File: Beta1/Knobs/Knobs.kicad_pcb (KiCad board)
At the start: 2 copper layers, 194 x 32.1 mm, 31 parts, among them U1000 MCP3008T-I/SL, U2 MCP3008T-I/SL

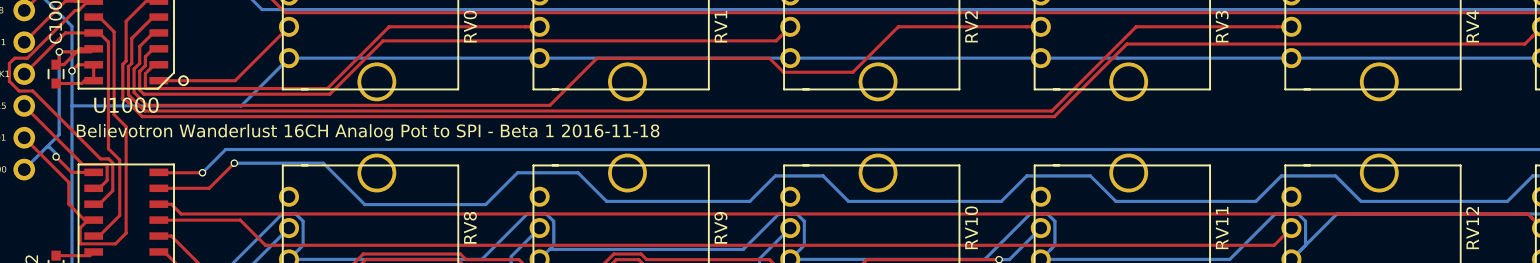
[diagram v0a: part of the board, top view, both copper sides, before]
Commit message: Housekeeping files. Renamed Knob with LED to Knobs. Board is ready for Gerbers.
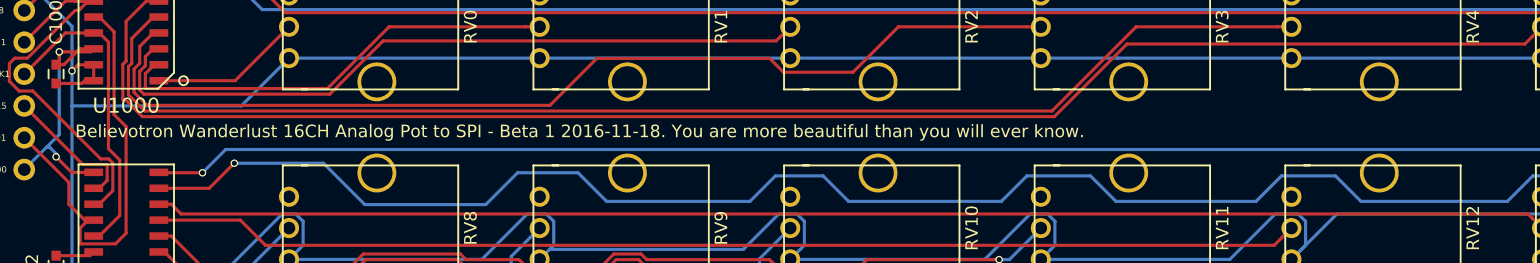
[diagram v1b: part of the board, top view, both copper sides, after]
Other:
- board text added: "Believotron Wanderlust 16CH Analog Pot to SPI - Beta 1 2016-11-18. You are more beautiful than you will ever know."
- board text removed: "Believotron Wanderlust 16CH Analog Pot to SPI - Beta 1 2016-11-18"
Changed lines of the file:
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@@
 (kicad_pcb (version 4) (host pcbnew 4.0.4-stable)
   (general
-    (links 0)
+    (links 68)
     (no_connects 0)
     (area -0.050001 -32.175001 194.010001 0.050001)
@@
     (pad "" np_thru_hole circle (at 0 0) (size 3.3 3.3) (drill 3.3) (layers *.Cu *.Mask))
   )
-  (gr_text "Believotron Wanderlust 16CH Analog Pot to SPI - Beta 1 2016-11-18" (at 11.684 -15.748) (layer F.SilkS)
+  (gr_text "Believotron Wanderlust 16CH Analog Pot to SPI - Beta 1 2016-11-18. You are more beautiful than you will ever know." (at 11.684 -15.748) (layer F.SilkS)
     (effects (font (size 1 1) (thickness 0.25)) (justify left))
   )

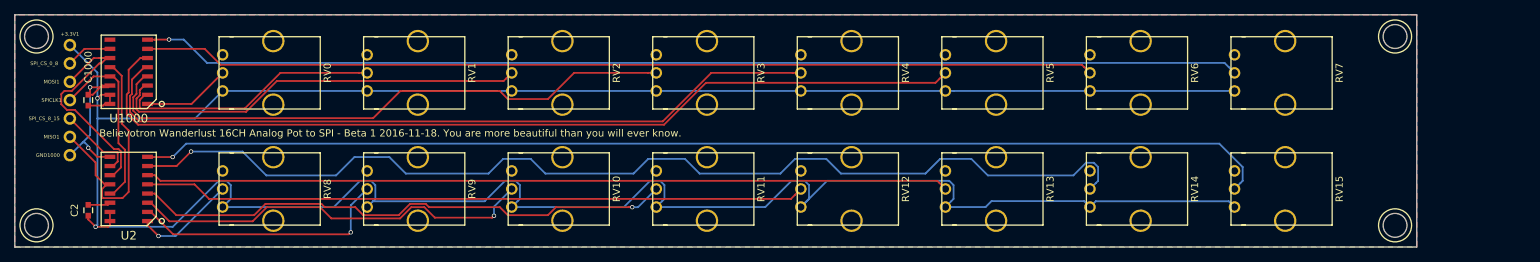
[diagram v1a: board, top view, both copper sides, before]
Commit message: Added second header row for easy daisychaining / interfacing
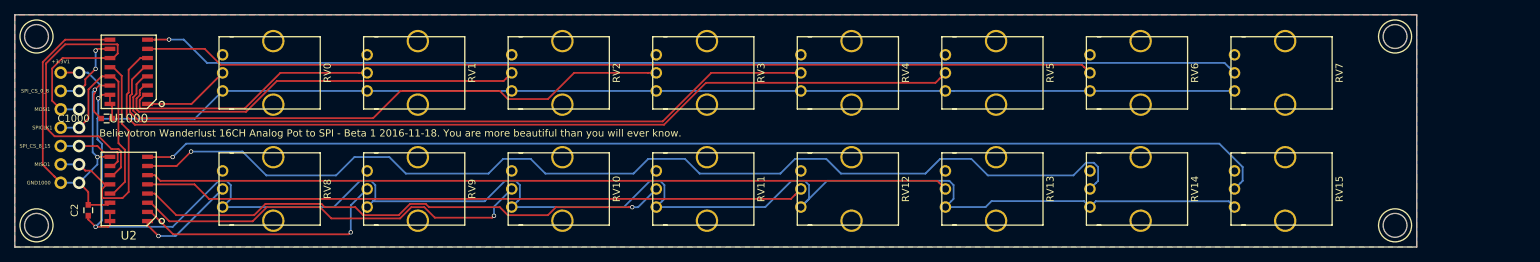
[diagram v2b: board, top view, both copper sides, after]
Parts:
- moved +3.3V1 4.02 mm to (6.35, -24.1)
- moved MISO1 4.02 mm to (6.35, -11.4)
- moved SPI_CS_8_15 4.02 mm to (6.35, -14.0)
- moved GND1000 4.02 mm to (6.35, -8.89)
- moved MOSI1 4.02 mm to (6.35, -19.1)
- moved SPICLK1 4.02 mm to (6.35, -16.5)
- moved SPI_CS_0_8 4.02 mm to (6.35, -21.6)
- moved C1000 3.59 mm to (12.7, -17.8), turned to 180 degrees
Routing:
- net GND: track 25.9 -> 60.6 mm, vias 2 -> 3
- net /Knobs/MOSI: track 34.2 -> 56.1 mm, vias 0 -> 1
- net /Knobs/SPICLK: track 25.4 -> 31.0 mm, vias 0 -> 1
- net /Knobs/CS_R0_7: track 6.37 -> 11.2 mm, vias 0 -> 3
- net /Knobs/MISO: track 34.5 -> 33.1 mm, vias 0 -> 1
- net +3V3: track 395.1 -> 393.8 mm, vias 2 -> 3
- net /Knobs/CS_LED_8_15: track 11.6 -> 11.3 mm, vias 0 -> 1

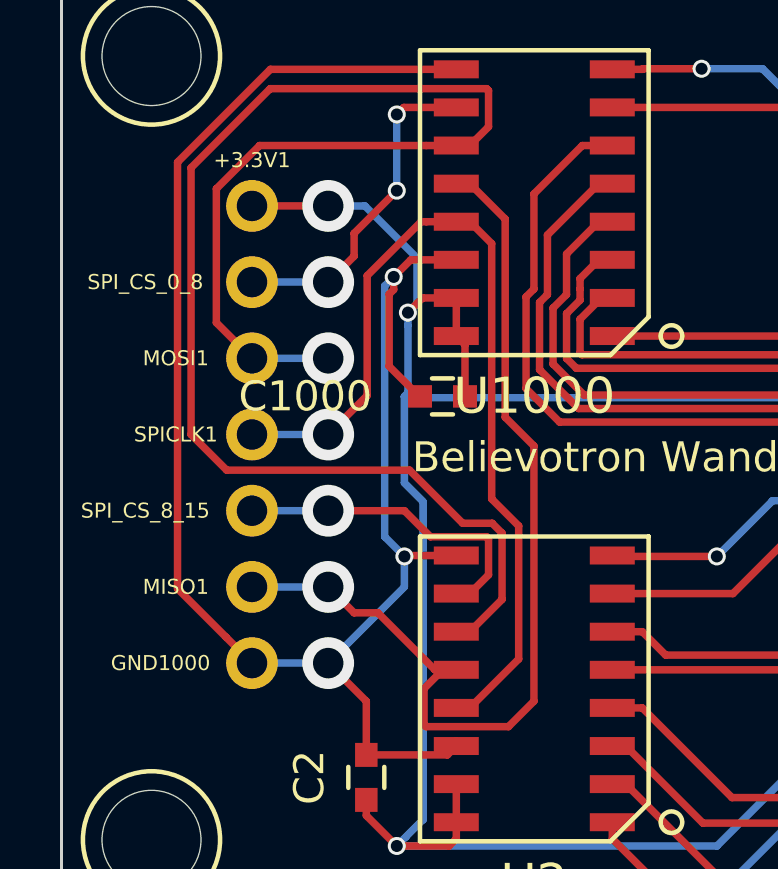
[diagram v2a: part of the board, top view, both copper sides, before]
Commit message: Changed second row daisy chain from vias to plated TH. You know. For kids.
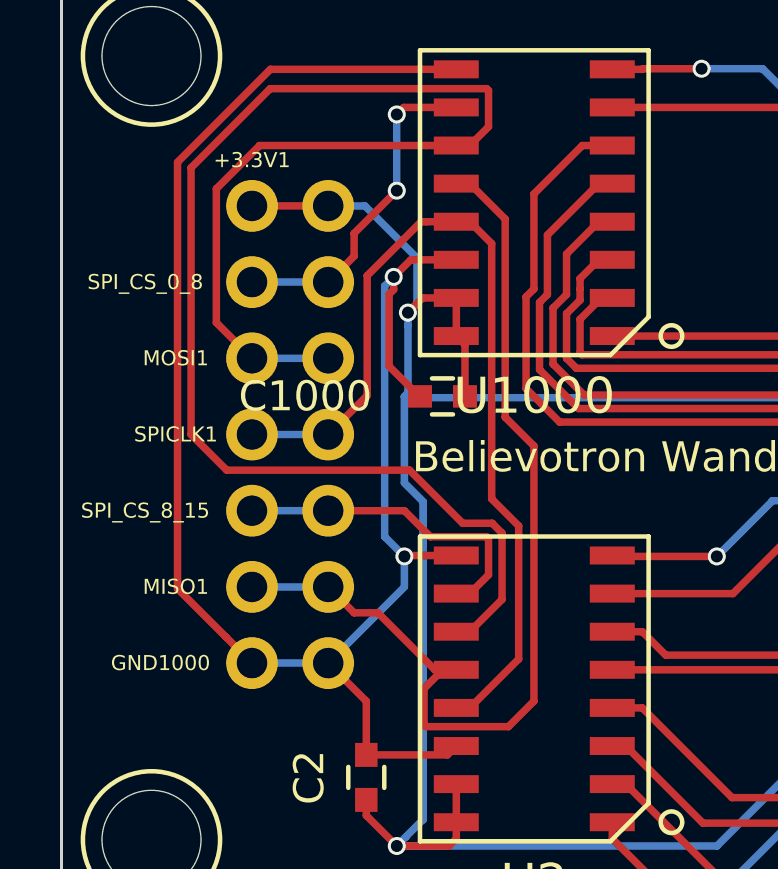
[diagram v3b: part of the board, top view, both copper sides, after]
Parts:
- added +3.3VB1: CONN_01X01, Liberry:single_0.1, F.Cu at (8.89, -24.1)
- added GNDB1000: CONN_01X01, Liberry:single_0.1, F.Cu at (8.89, -8.89)
- added MISOB1: CONN_01X01, Liberry:single_0.1, F.Cu at (8.89, -11.4)
- added MOSIB1: CONN_01X01, Liberry:single_0.1, F.Cu at (8.89, -19.1)
- added SPICLKB1: CONN_01X01, Liberry:single_0.1, F.Cu at (8.89, -16.5)
- added SPI_CSB_0_8: CONN_01X01, Liberry:single_0.1, F.Cu at (8.89, -21.6)
- added SPI_CSB_8_15: CONN_01X01, Liberry:single_0.1, F.Cu at (8.89, -14.0)
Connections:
- net /Knobs/CS_LED_8_15 renamed /CS_LED_8_15
- net /Knobs/CS_R0_7 renamed /CS_R0_7
- net /Knobs/MISO renamed /MISO
- net /Knobs/MOSI renamed /MOSI
- net /Knobs/P0 renamed /P0
- net /Knobs/P1 renamed /P1
- net /Knobs/P10 renamed /P10
- net /Knobs/P11 renamed /P11
- net /Knobs/P12 renamed /P12
- net /Knobs/P13 renamed /P13
- net /Knobs/P14 renamed /P14
- net /Knobs/P15 renamed /P15
- net /Knobs/P2 renamed /P2
- net /Knobs/P3 renamed /P3
- net /Knobs/P4 renamed /P4
- net /Knobs/P5 renamed /P5
- net /Knobs/P6 renamed /P6
- net /Knobs/P7 renamed /P7
- net /Knobs/P8 renamed /P8
- net /Knobs/P9 renamed /P9
- net /Knobs/SPICLK renamed /SPICLK
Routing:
- net GND: vias 3 -> 2
- net /SPICLK: vias 1 -> 0
- net /MOSI: vias 1 -> 0
- net /MISO: vias 1 -> 0
- net /CS_R0_7: vias 3 -> 2
- net /CS_LED_8_15: vias 1 -> 0
- net +3V3: vias 3 -> 2

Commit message: Added PCB #
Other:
- board text added: "PCBBTWL_KN16 Beta 1 2016-11-18 Believotron Wanderlust 16CH Analog Pot to SPI. You are more beautiful than you will ever know."
- board text removed: "Believotron Wanderlust 16CH Analog Pot to SPI - Beta 1 2016-11-18. You are more beautiful than you will ever know."
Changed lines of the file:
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@@
     (links 75)
     (no_connects 0)
-    (area -0.050001 -32.175001 194.010001 0.050001)
+    (area -0.325001 -33.148 194.285002 0.869)
     (thickness 1.6)
     (drawings 15)
@@
       (net 23 /CS_LED_8_15))
   )
-  (gr_text "Believotron Wanderlust 16CH Analog Pot to SPI - Beta 1 2016-11-18. You are more beautiful than you will ever know." (at 11.684 -15.748) (layer F.SilkS)
+  (gr_text "PCBBTWL_KN16 Beta 1 2016-11-18 Believotron Wanderlust 16CH Analog Pot to SPI. You are more beautiful than you will ever know." (at 11.684 -15.748) (layer F.SilkS)
     (effects (font (size 1 1) (thickness 0.25)) (justify left))
   )

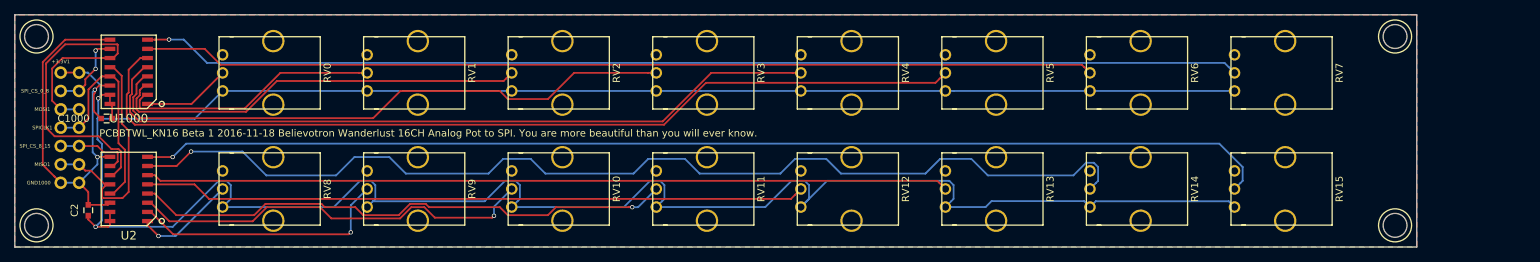
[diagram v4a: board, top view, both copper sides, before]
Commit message: Catchup Commit.  Non-atomic, Refactored LED, Keyboard, KeyPAD, and Knobs PCBs
LED: Changed chips. Cleaned up silkscreen text. Added some support
mounting holes. Shrank height of board to avoid stackup. KeyPAD is
updated with new footprint. Keyboard and Knobs are unknown.
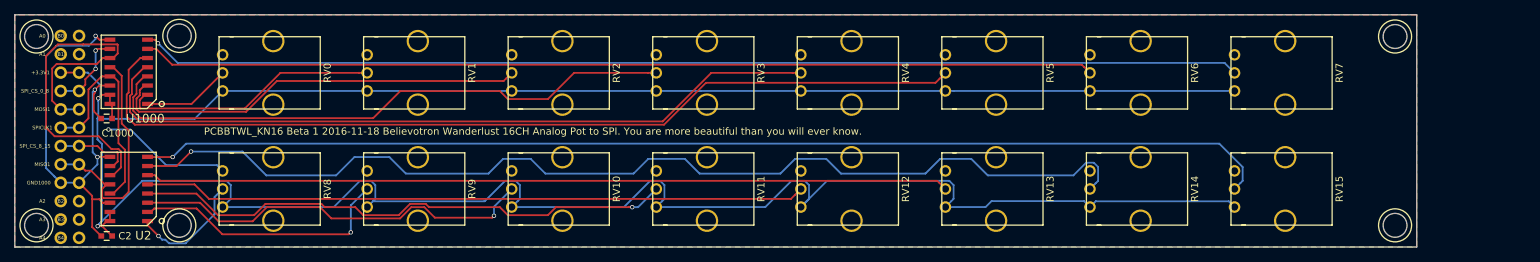
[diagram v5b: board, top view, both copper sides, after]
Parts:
- added A0: CONN_01X01, Liberry:single_0.1, F.Cu at (6.35, -29.2)
- added A1: CONN_01X01, Liberry:single_0.1, F.Cu at (6.35, -26.7)
- added A2: CONN_01X01, Liberry:single_0.1, F.Cu at (6.35, -6.35)
- added A3: CONN_01X01, Liberry:single_0.1, F.Cu at (6.35, -3.81)
- added A4: CONN_01X01, Liberry:single_0.1, F.Cu at (6.35, -1.27)
- added B0: CONN_01X01, Liberry:single_0.1, F.Cu at (8.89, -29.2)
- added B1: CONN_01X01, Liberry:single_0.1, F.Cu at (8.89, -26.7)
- added B2: CONN_01X01, Liberry:single_0.1, F.Cu at (8.89, -6.35)
- added B3: CONN_01X01, Liberry:single_0.1, F.Cu at (8.89, -3.81)
- added B4: CONN_01X01, Liberry:single_0.1, F.Cu at (8.89, -1.27)
- added REF**: 1pin, Connect:1pin, F.Cu at (22.8, -29.2)
- added REF**: 1pin, Connect:1pin, F.Cu at (22.8, -3.00)
- moved C2 4.38 mm to (12.7, -1.52), turned to 180 degrees
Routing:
- net GND: track 60.6 -> 83.7 mm, vias 2 -> 4
- net /P8: track 14.3 -> 16.7 mm
- net +3V3: track 393.8 -> 392.7 mm
- net /MOSI: track 56.1 -> 56.7 mm

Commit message: Reduced Height, Moved TH, Holes, SMT Chips, Rerouted.
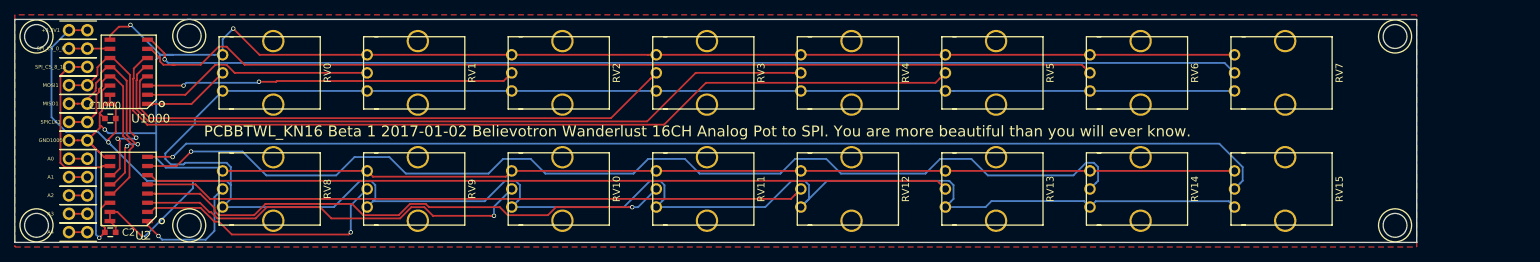
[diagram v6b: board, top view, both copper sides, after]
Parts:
- removed +3.3VB1, B0, B1, B2, B3, B4, GNDB1000, MISOB1, MOSIB1, SPICLKB1, SPI_CSB_0_8, SPI_CSB_8_15: CONN_01X01, Liberry:single_0.1
- +3.3V1, A0, A1, A2, A3, A4, GND1000, MISO1, MOSI1, SPICLK1, SPI_CS_0_8, SPI_CS_8_15: footprint Liberry:single_0.1 -> Liberry:TH_0.1_1x2_Jumper
- moved A0 17.0 mm to (7.49, -12.2)
- moved A1 17.0 mm to (7.49, -9.68)
- moved SPI_CS_8_15 11.0 mm to (7.49, -24.9)
- moved MISO1 8.48 mm to (7.49, -19.8)
- moved +3.3V1 5.98 mm to (7.49, -30.0)
- moved GND1000 5.98 mm to (7.49, -14.8)
- moved SPI_CS_0_8 5.98 mm to (7.49, -27.5)
- moved MOSI1 3.52 mm to (7.49, -22.4)
- moved A2 1.39 mm to (7.49, -7.14)
- moved A3 1.39 mm to (7.49, -4.60)
- moved A4 1.39 mm to (7.49, -2.06)
- moved SPICLK1 1.39 mm to (7.49, -17.3)
- moved REF** 1.37 mm to (24.1, -29.2)
- moved REF** 1.37 mm to (24.1, -3.00)
- moved C2 0.71 mm to (13.2, -2.03)
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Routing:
- net GND: track 83.7 -> 374.9 mm
- net /MOSI: track 56.7 -> 29.3 mm, vias 0 -> 2
- net +3V3: track 392.7 -> 412.3 mm
- net /CS_LED_8_15: track 11.3 -> 23.5 mm
- net /P2: track 58.5 -> 51.6 mm, vias 0 -> 2
- net /CS_R0_7: track 11.2 -> 5.69 mm, vias 2 -> 0
- net /MISO: track 33.1 -> 29.9 mm, vias 0 -> 2
- net /P1: track 36.0 -> 32.9 mm
- net /P6: track 131.8 -> 134.4 mm
- net Net-(A4-Pad1): track 0.00 -> 2.54 mm
- net Net-(A3-Pad1): track 0.00 -> 2.54 mm
- net Net-(A2-Pad1): track 0.00 -> 2.54 mm
- net Net-(A1-Pad1): track 0.00 -> 2.54 mm
- net Net-(A0-Pad1): track 0.00 -> 2.54 mm
- net /P3: track 82.1 -> 79.7 mm
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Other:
- board size 194 x 32.1 mm -> 194 x 30.9 mm
- board text added: "PCBBTWL_KN16 Beta 1 2017-01-02 Believotron Wanderlust 16CH Analog Pot to SPI. You are more beautiful than you will ever know."
- board text removed: "PCBBTWL_KN16 Beta 1 2016-11-18 Believotron Wanderlust 16CH Analog Pot to SPI. You are more beautiful than you will ever know."
